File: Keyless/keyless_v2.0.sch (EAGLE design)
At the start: 45 parts, among them J1 AVR_SPI_PRG_6NS, U1 USD-SOCKET, X1 USB-SMD-NS, Y1 16MHz

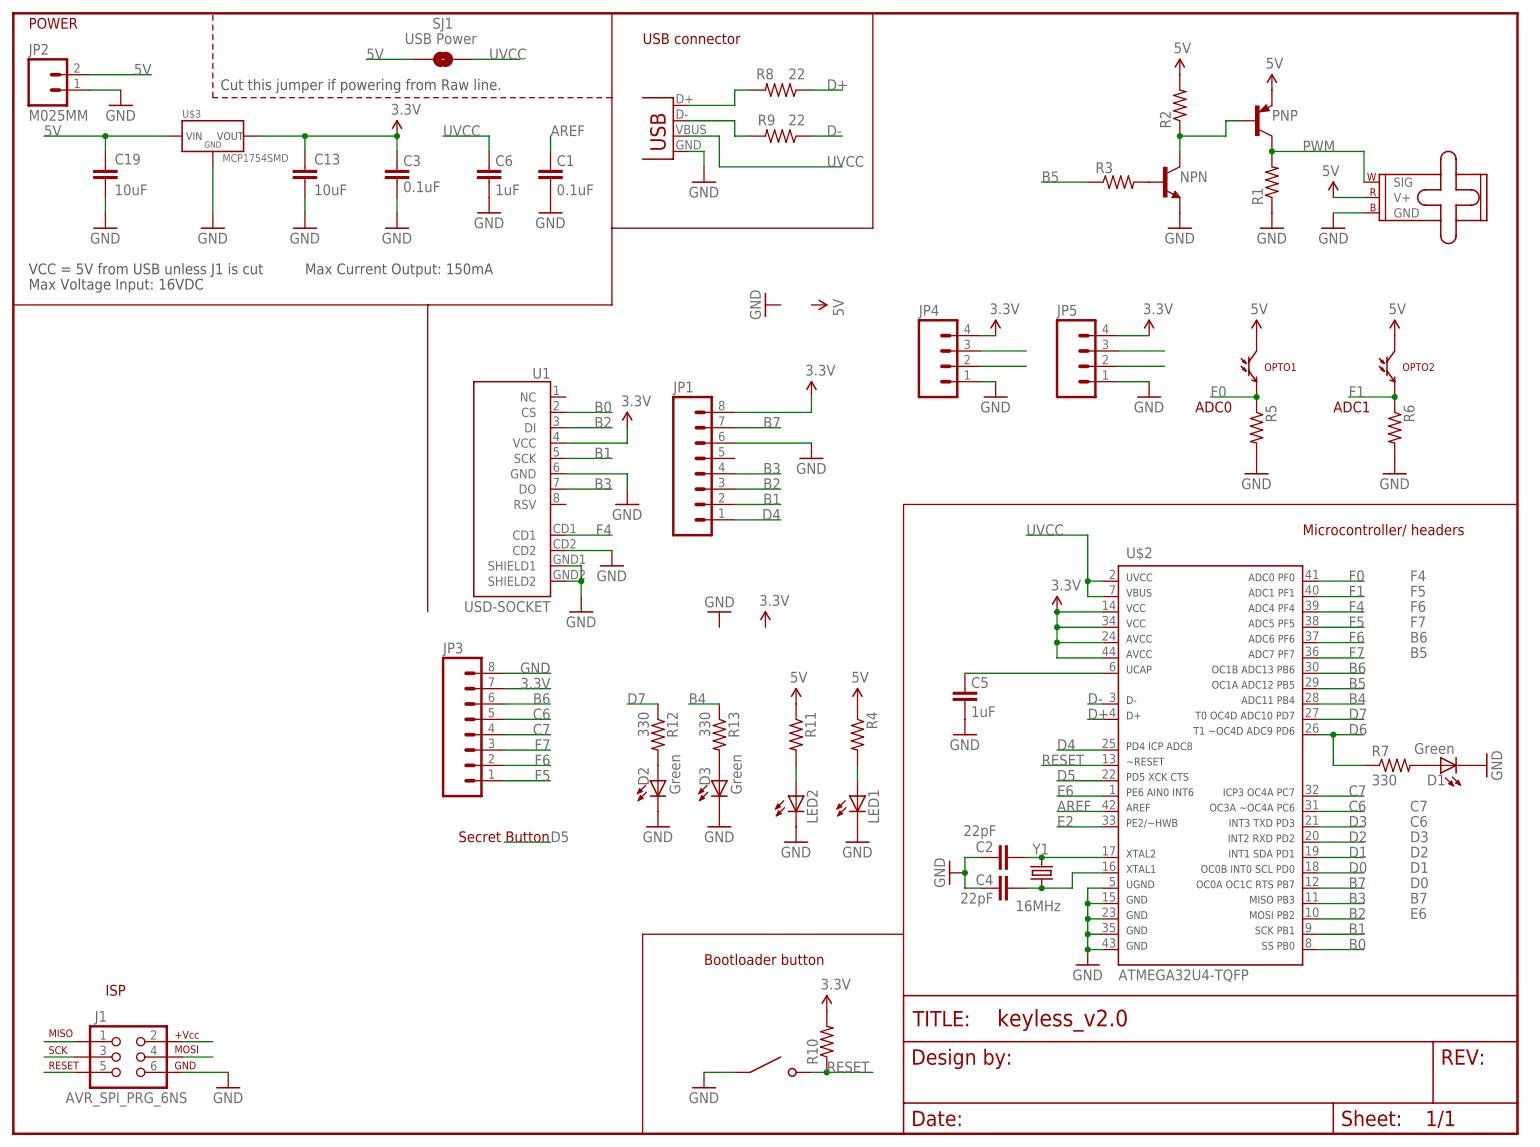
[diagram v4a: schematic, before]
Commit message: added values & BOM
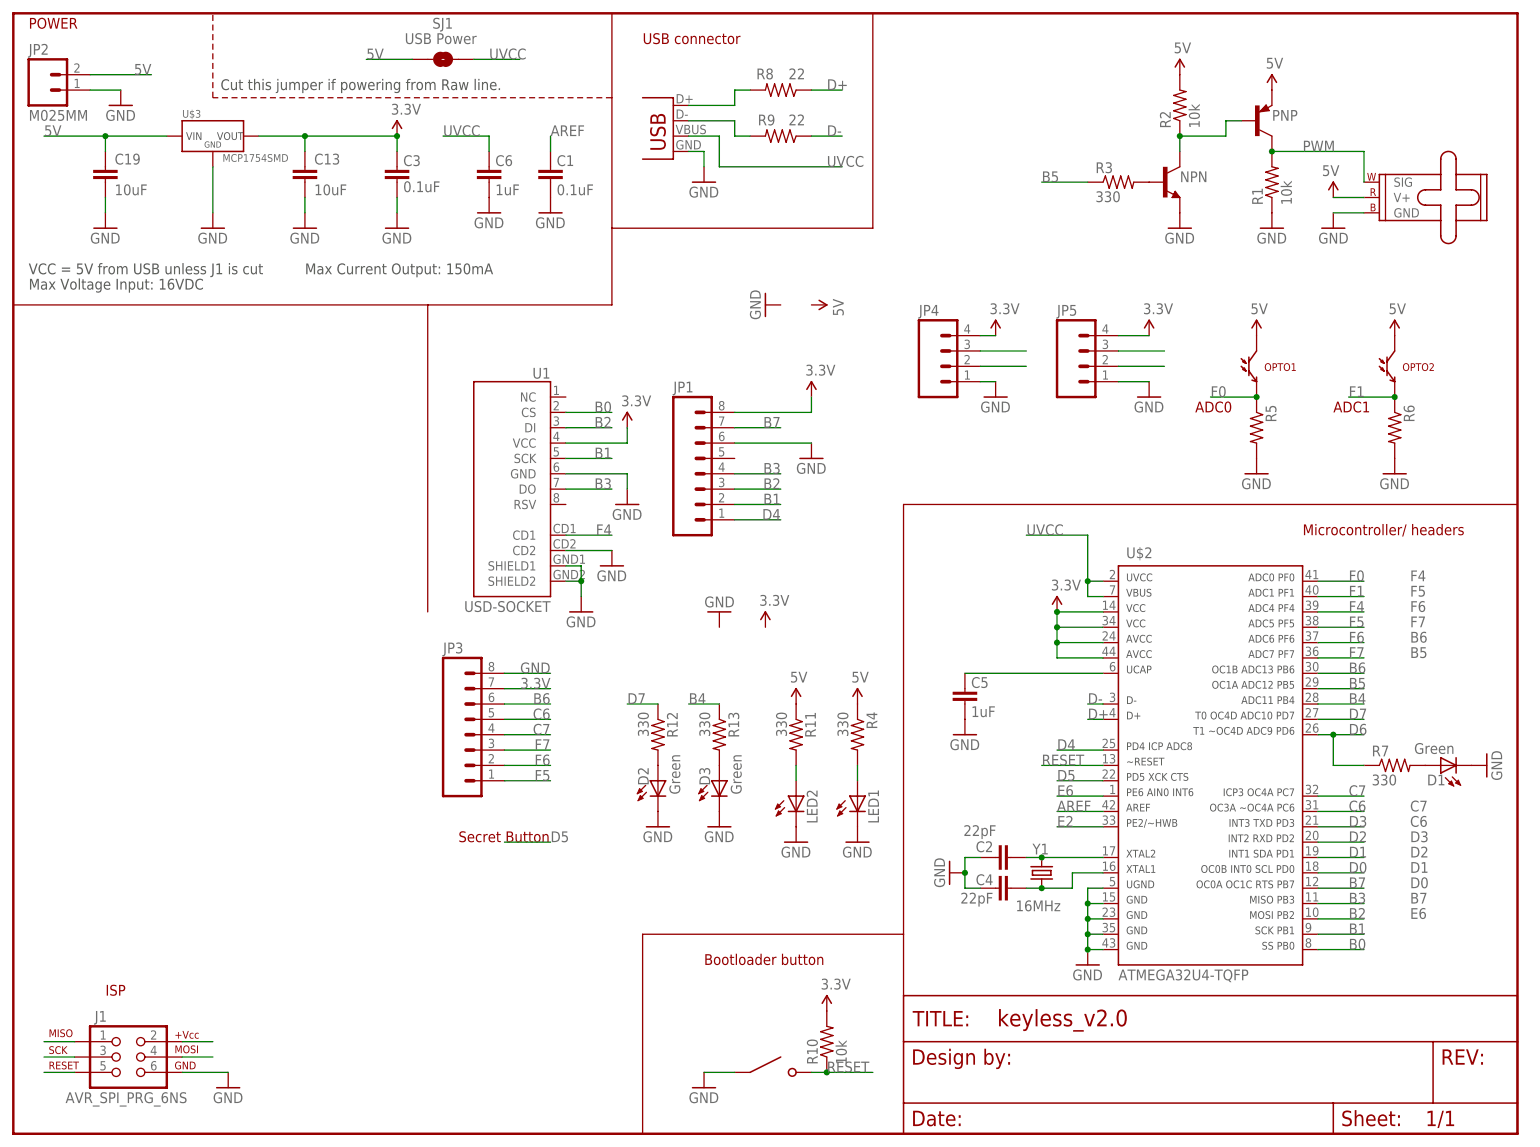
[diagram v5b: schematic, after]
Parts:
- R1, R10, R2: value (none) -> 10k
- R11, R3, R4: value (none) -> 330
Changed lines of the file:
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@@
 <part name="SUPPLY5" library="SparkFun-Aesthetics" deviceset="5V" device=""/>
 <part name="SUPPLY7" library="SparkFun-Aesthetics" deviceset="5V" device=""/>
-<part name="R1" library="SparkFun-Passives" deviceset="RESISTOR" device="AXIAL-0.3"/>
-<part name="R2" library="SparkFun-Passives" deviceset="RESISTOR" device="AXIAL-0.3"/>
-<part name="R3" library="SparkFun-Passives" deviceset="RESISTOR" device="AXIAL-0.3"/>
-<part name="R4" library="SparkFun-Passives" deviceset="RESISTOR" device="AXIAL-0.3"/>
+<part name="R1" library="SparkFun-Passives" deviceset="RESISTOR" device="AXIAL-0.3" value="10k"/>
+<part name="R2" library="SparkFun-Passives" deviceset="RESISTOR" device="AXIAL-0.3" value="10k"/>
+<part name="R3" library="SparkFun-Passives" deviceset="RESISTOR" device="AXIAL-0.3" value="330"/>
+<part name="R4" library="SparkFun-Passives" deviceset="RESISTOR" device="AXIAL-0.3" value="330"/>
 <part name="R5" library="SparkFun-Passives" deviceset="RESISTOR" device="AXIAL-0.3"/>
 <part name="R6" library="SparkFun-Passives" deviceset="RESISTOR" device="AXIAL-0.3"/>
@@
 <part name="U$1" library="Homebrew" deviceset="MINI-SPDT" device=""/>
 <part name="GND5" library="SparkFun" deviceset="GND" device=""/>
-<part name="R10" library="resistor" deviceset="R-US_" device="R0603"/>
+<part name="R10" library="resistor" deviceset="R-US_" device="R0603" value="10k"/>
 <part name="P+1" library="SparkFun" deviceset="3.3V" device=""/>
 <part name="P+2" library="SparkFun" deviceset="3.3V" device=""/>
@@
 <part name="GND20" library="SparkFun-Aesthetics" deviceset="GND" device=""/>
 <part name="GND21" library="SparkFun-Aesthetics" deviceset="GND" device=""/>
-<part name="R11" library="SparkFun-Passives" deviceset="RESISTOR" device="AXIAL-0.3"/>
+<part name="R11" library="SparkFun-Passives" deviceset="RESISTOR" device="AXIAL-0.3" value="330"/>
 <part name="LED2" library="led" deviceset="LED" device="5MM"/>
 <part name="SUPPLY3" library="SparkFun-Aesthetics" deviceset="5V" device=""/>
